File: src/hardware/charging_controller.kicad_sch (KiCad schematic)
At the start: 19 parts, among them J82 Conn_01x02_Pin, J83 Conn_01x04_Pin, J84 Conn_02x08_Top_Bottom, J85 Conn_02x08_Top_Bottom, J86 Conn_01x02_Pin, J87 Conn_01x01_Pin, U31 TPS22916BYFPR, U32 BQ25185DLHR

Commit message: Fixed U32
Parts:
- U32: footprint BQ25185DLHR:IC_BQ25185DLHR -> Project:IC_BQ25185DLHR
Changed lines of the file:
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@@
 			)
 		)
-		(property "Footprint" "BQ25185DLHR:IC_BQ25185DLHR"
+		(property "Footprint" "Project:IC_BQ25185DLHR"
 			(at 147.32 101.6 0)
 			(effects

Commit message: Changed pin headers to vertical
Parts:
- J82, J86: footprint Connector_PinHeader_2.54mm:PinHeader_1x02_P2.54mm_Horizontal -> Connector_PinHeader_2.54mm:PinHeader_1x02_P2.54mm_Vertical
- J83: footprint Connector_PinHeader_2.54mm:PinHeader_1x04_P2.54mm_Horizontal -> Connector_PinHeader_2.54mm:PinHeader_1x04_P2.54mm_Vertical
- J87: footprint Connector_PinHeader_2.54mm:PinHeader_1x01_P2.54mm_Horizontal -> Connector_PinHeader_2.54mm:PinHeader_1x04_P2.54mm_Vertical
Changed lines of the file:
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@@
 			)
 		)
-		(property "Footprint" "Connector_PinHeader_2.54mm:PinHeader_1x01_P2.54mm_Horizontal"
+		(property "Footprint" "Connector_PinHeader_2.54mm:PinHeader_1x04_P2.54mm_Vertical"
 			(at 200.66 48.26 0)
 			(effects
@@
 			)
 		)
-		(property "Footprint" "Connector_PinHeader_2.54mm:PinHeader_1x02_P2.54mm_Horizontal"
+		(property "Footprint" "Connector_PinHeader_2.54mm:PinHeader_1x02_P2.54mm_Vertical"
 			(at 74.93 44.45 0)
 			(effects
@@
 			)
 		)
-		(property "Footprint" "Connector_PinHeader_2.54mm:PinHeader_1x02_P2.54mm_Horizontal"
+		(property "Footprint" "Connector_PinHeader_2.54mm:PinHeader_1x02_P2.54mm_Vertical"
 			(at 200.66 39.37 0)
 			(effects
@@
 			)
 		)
-		(property "Footprint" "Connector_PinHeader_2.54mm:PinHeader_1x04_P2.54mm_Horizontal"
+		(property "Footprint" "Connector_PinHeader_2.54mm:PinHeader_1x04_P2.54mm_Vertical"
 			(at 74.93 54.61 0)
 			(effects

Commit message: Fixed connector footprints; Changed conectors from 2.54 to 1.27
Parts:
- J80: renamed from J82; footprint Connector_PinHeader_2.54mm:PinHeader_1x02_P2.54mm_Vertical -> Connector_PinHeader_1.27mm:PinHeader_1x02_P1.27mm_Vertical
- J81: renamed from J83; footprint Connector_PinHeader_2.54mm:PinHeader_1x04_P2.54mm_Vertical -> Connector_PinHeader_1.27mm:PinHeader_1x04_P1.27mm_Vertical
- J82: renamed from J84; footprint Connector_PinHeader_2.54mm:PinHeader_2x08_P2.54mm_Vertical -> Connector_PinHeader_1.27mm:PinHeader_2x08_P1.27mm_Vertical
- J83: renamed from J85; footprint Connector_PinHeader_2.54mm:PinHeader_2x08_P2.54mm_Vertical -> Connector_PinHeader_1.27mm:PinHeader_2x08_P1.27mm_Vertical
- J84: renamed from J86; footprint Connector_PinHeader_2.54mm:PinHeader_1x02_P2.54mm_Vertical -> Connector_PinHeader_1.27mm:PinHeader_1x02_P1.27mm_Vertical
- J85: renamed from J87; footprint Connector_PinHeader_2.54mm:PinHeader_1x04_P2.54mm_Vertical -> Connector_PinHeader_1.27mm:PinHeader_1x01_P1.27mm_Vertical
- renumbered R33 to R34, R34 to R35, R35 to R36, R36 to R37, R37 to R38

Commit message: Fixes; Added TPM PCB
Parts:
- C71, C72, C73, C74, C75, C76: footprint Capacitor_SMD:C_0504_1310Metric -> Capacitor_SMD:C_0402_1005Metric
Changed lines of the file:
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@@
 			)
 		)
-		(property "Footprint" "Capacitor_SMD:C_0504_1310Metric"
+		(property "Footprint" "Capacitor_SMD:C_0402_1005Metric"
 			(at 126.6952 74.93 0)
 			(effects
@@
 			)
 		)
-		(property "Footprint" "Capacitor_SMD:C_0504_1310Metric"
+		(property "Footprint" "Capacitor_SMD:C_0402_1005Metric"
 			(at 178.1048 91.44 0)
 			(effects
@@
 			)
 		)
-		(property "Footprint" "Capacitor_SMD:C_0504_1310Metric"
+		(property "Footprint" "Capacitor_SMD:C_0402_1005Metric"
 			(at 167.9448 74.93 0)
 			(effects
@@
 			)
 		)
-		(property "Footprint" "Capacitor_SMD:C_0504_1310Metric"
+		(property "Footprint" "Capacitor_SMD:C_0402_1005Metric"
 			(at 178.1048 74.93 0)
 			(effects
@@
 			)
 		)
-		(property "Footprint" "Capacitor_SMD:C_0504_1310Metric"
+		(property "Footprint" "Capacitor_SMD:C_0402_1005Metric"
 			(at 116.5352 74.93 0)
 			(effects
@@
 			)
 		)
-		(property "Footprint" "Capacitor_SMD:C_0504_1310Metric"
+		(property "Footprint" "Capacitor_SMD:C_0402_1005Metric"
 			(at 167.9448 91.44 0)
 			(effects

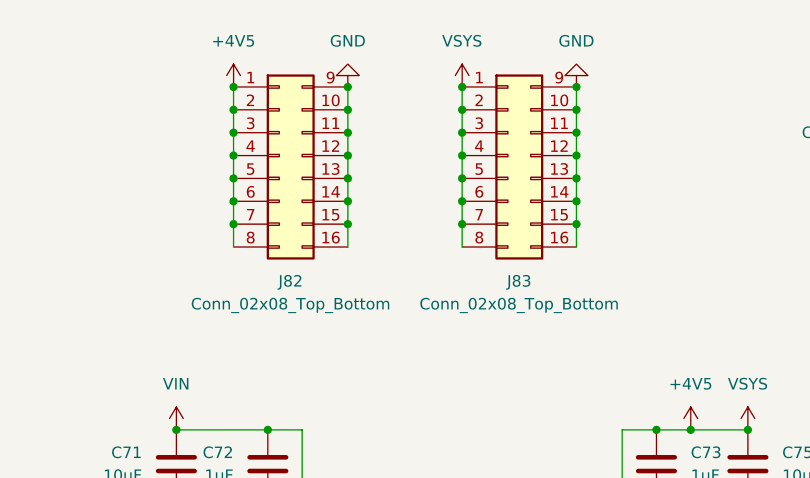
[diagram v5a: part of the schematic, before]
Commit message: Fixed 02x08 connector symbol
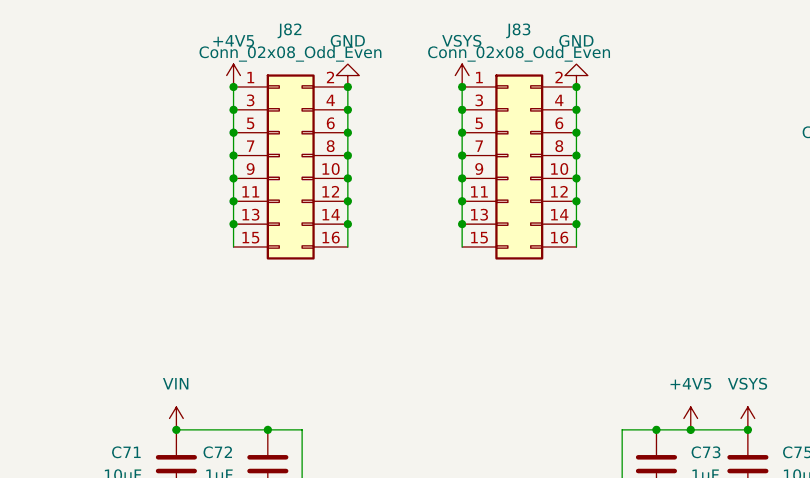
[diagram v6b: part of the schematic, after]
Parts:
- removed J82, J83: Conn_02x08_Top_Bottom, Connector_PinHeader_1.27mm:PinHeader_2x08_P1.27mm_Vertical, symbol Connector_Generic:Conn_02x08_Top_Bottom
- added J82, J83: Conn_02x08_Odd_Even, symbol Connector_Generic:Conn_02x08_Odd_Even
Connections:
- net +4V5: now also J82.1 (Pin_1), J82.11 (Pin_11), J82.13 (Pin_13), J82.15 (Pin_15), J82.3 (Pin_3), J82.5 (Pin_5), J82.7 (Pin_7), J82.9 (Pin_9), J83.1 (Pin_1), J83.11 (Pin_11), J83.13 (Pin_13), J83.15 (Pin_15), J83.3 (Pin_3), J83.5 (Pin_5), J83.7 (Pin_7), J83.9 (Pin_9)
- net GND: now also J82.10 (Pin_10), J82.12 (Pin_12), J82.14 (Pin_14), J82.16 (Pin_16), J82.2 (Pin_2), J82.4 (Pin_4), J82.6 (Pin_6), J82.8 (Pin_8), J83.10 (Pin_10), J83.12 (Pin_12), J83.14 (Pin_14), J83.16 (Pin_16), J83.2 (Pin_2), J83.4 (Pin_4), J83.6 (Pin_6), J83.8 (Pin_8)

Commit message: Applied fixes
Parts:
- J82, J83: footprint (none) -> Connector_PinHeader_1.27mm:PinHeader_2x08_P1.27mm_Vertical
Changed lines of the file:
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@@
 			)
 		)
-		(property "Footprint" ""
+		(property "Footprint" "Connector_PinHeader_1.27mm:PinHeader_2x08_P1.27mm_Vertical"
 			(at 127 44.45 0)
 			(effects
@@
 			)
 		)
-		(property "Footprint" ""
+		(property "Footprint" "Connector_PinHeader_1.27mm:PinHeader_2x08_P1.27mm_Vertical"
 			(at 152.4 44.45 0)
 			(effects
